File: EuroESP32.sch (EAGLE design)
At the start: 127 parts, among them IC1 TL074D, IC10 MCP6004, IC2 TL072, IC3 TL072, IC4 WM8731, IC5 TL074D, IC7 ADP7118, P4 POWER_SIMPLE10, U1 LM4040SOT23, U2 MCP3204-CI/SL

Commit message: A few corrections
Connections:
- removed net LHPOUT: IC4.LHPOUT
- removed net MICBIAS: IC4.MICBIAS
- removed net MICIN: IC4.MICIN
- removed net RHPOUT: IC4.RHPOUT
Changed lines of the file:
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@@
-</segment>
-</net>
-<net name="LHPOUT" class="0">
-<segment>
-<pinref part="IC4" gate="G$1" pin="LHPOUT"/>
-<wire x1="76.2" y1="-55.88" x2="78.74" y2="-55.88" width="0.1524" layer="91"/>
-<label x="78.74" y="-55.88" size="1.778" layer="95" xref="yes"/>
-</segment>
-</net>
-<net name="RHPOUT" class="0">
-<segment>
-<pinref part="IC4" gate="G$1" pin="RHPOUT"/>
-<wire x1="76.2" y1="-58.42" x2="93.98" y2="-58.42" width="0.1524" layer="91"/>
-<label x="93.98" y="-58.42" size="1.778" layer="95" xref="yes"/>
 </segment>
 </net>
@@
 <wire x1="104.14" y1="-124.46" x2="106.68" y2="-124.46" width="0.1524" layer="91"/>
 <label x="106.68" y="-124.46" size="1.778" layer="95" xref="yes"/>
-</segment>
-</net>
-<net name="MICIN" class="0">
-<segment>
-<pinref part="IC4" gate="G$1" pin="MICIN"/>
-<wire x1="76.2" y1="-71.12" x2="78.74" y2="-71.12" width="0.1524" layer="91"/>
-<label x="78.74" y="-71.12" size="1.778" layer="95" xref="yes"/>
-</segment>
-</net>
-<net name="MICBIAS" class="0">
-<segment>
-<pinref part="IC4" gate="G$1" pin="MICBIAS"/>
-<wire x1="76.2" y1="-73.66" x2="93.98" y2="-73.66" width="0.1524" layer="91"/>
-<label x="93.98" y="-73.66" size="1.778" layer="95" xref="yes"/>
 </segment>
 </net>
@@
 </segment>
 </net>
-<net name="N$7" class="0">
-<segment>
-<pinref part="R21" gate="G$1" pin="1"/>
-<wire x1="421.64" y1="-58.42" x2="416.56" y2="-58.42" width="0.1524" layer="91"/>
-<wire x1="416.56" y1="-58.42" x2="416.56" y2="-68.58" width="0.1524" layer="91"/>
-<pinref part="IC1" gate="B" pin="-IN"/>
-<pinref part="R20" gate="G$1" pin="2"/>
-<wire x1="416.56" y1="-68.58" x2="421.64" y2="-68.58" width="0.1524" layer="91"/>
-<wire x1="411.48" y1="-68.58" x2="416.56" y2="-68.58" width="0.1524" layer="91"/>
-</segment>
-</net>
 <net name="N$8" class="0">
 <segment>
@@
 </segment>
 </net>
-<net name="N$10" class="0">
-<segment>
-<wire x1="421.64" y1="-81.28" x2="416.56" y2="-81.28" width="0.1524" layer="91"/>
-<wire x1="416.56" y1="-81.28" x2="416.56" y2="-91.44" width="0.1524" layer="91"/>
-<wire x1="416.56" y1="-91.44" x2="424.18" y2="-91.44" width="0.1524" layer="91"/>
-<wire x1="411.48" y1="-91.44" x2="416.56" y2="-91.44" width="0.1524" layer="91"/>
-<pinref part="R25" gate="G$1" pin="2"/>
-<pinref part="R26" gate="G$1" pin="1"/>
-<pinref part="IC1" gate="D" pin="-IN"/>
-</segment>
-</net>
 <net name="N$11" class="0">
 <segment>
@@
 </segment>
 </net>
-<net name="N$14" class="0">
-<segment>
-<pinref part="R31" gate="G$1" pin="1"/>
-<wire x1="421.64" y1="-121.92" x2="416.56" y2="-121.92" width="0.1524" layer="91"/>
-<wire x1="416.56" y1="-121.92" x2="416.56" y2="-132.08" width="0.1524" layer="91"/>
-<pinref part="IC5" gate="B" pin="-IN"/>
-<pinref part="R30" gate="G$1" pin="2"/>
-<wire x1="416.56" y1="-132.08" x2="421.64" y2="-132.08" width="0.1524" layer="91"/>
-<wire x1="411.48" y1="-132.08" x2="416.56" y2="-132.08" width="0.1524" layer="91"/>
-</segment>
-</net>
 <net name="N$16" class="0">
 <segment>
@@
 <pinref part="R38" gate="G$1" pin="1"/>
 <pinref part="IC5" gate="D" pin="OUT"/>
-</segment>
-</net>
-<net name="N$22" class="0">
-<segment>
-<wire x1="421.64" y1="-144.78" x2="416.56" y2="-144.78" width="0.1524" layer="91"/>
-<wire x1="416.56" y1="-144.78" x2="416.56" y2="-154.94" width="0.1524" layer="91"/>
-<wire x1="416.56" y1="-154.94" x2="424.18" y2="-154.94" width="0.1524" layer="91"/>
-<wire x1="411.48" y1="-154.94" x2="416.56" y2="-154.94" width="0.1524" layer="91"/>
-<pinref part="R36" gate="G$1" pin="2"/>
-<pinref part="R37" gate="G$1" pin="1"/>
-<pinref part="IC5" gate="D" pin="-IN"/>
 </segment>
 </net>
@@
 </segment>
 </net>
+<net name="N$28" class="0">
+<segment>
+<pinref part="R26" gate="G$1" pin="1"/>
+<wire x1="421.64" y1="-81.28" x2="416.56" y2="-81.28" width="0.1524" layer="91"/>
+<wire x1="411.48" y1="-91.44" x2="416.56" y2="-91.44" width="0.1524" layer="91"/>
+<pinref part="R25" gate="G$1" pin="2"/>
+<pinref part="IC1" gate="D" pin="-IN"/>
+<wire x1="416.56" y1="-91.44" x2="424.18" y2="-91.44" width="0.1524" layer="91"/>
+<wire x1="416.56" y1="-81.28" x2="416.56" y2="-91.44" width="0.1524" layer="91"/>
+<junction x="416.56" y="-91.44"/>
+</segment>
+</net>
+<net name="N$10" class="0">
+<segment>
+<pinref part="R31" gate="G$1" pin="1"/>
+<wire x1="421.64" y1="-121.92" x2="416.56" y2="-121.92" width="0.1524" layer="91"/>
+<pinref part="IC5" gate="B" pin="-IN"/>
+<pinref part="R30" gate="G$1" pin="2"/>
+<wire x1="411.48" y1="-132.08" x2="416.56" y2="-132.08" width="0.1524" layer="91"/>
+<wire x1="416.56" y1="-132.08" x2="421.64" y2="-132.08" width="0.1524" layer="91"/>
+<wire x1="416.56" y1="-121.92" x2="416.56" y2="-132.08" width="0.1524" layer="91"/>
+<junction x="416.56" y="-132.08"/>
+</segment>
+</net>
+<net name="N$14" class="0">
+<segment>
+<pinref part="R37" gate="G$1" pin="1"/>
+<wire x1="421.64" y1="-144.78" x2="416.56" y2="-144.78" width="0.1524" layer="91"/>
+<wire x1="411.48" y1="-154.94" x2="416.56" y2="-154.94" width="0.1524" layer="91"/>
+<pinref part="R36" gate="G$1" pin="2"/>
+<pinref part="IC5" gate="D" pin="-IN"/>
+<wire x1="416.56" y1="-154.94" x2="424.18" y2="-154.94" width="0.1524" layer="91"/>
+<wire x1="416.56" y1="-144.78" x2="416.56" y2="-154.94" width="0.1524" layer="91"/>
+<junction x="416.56" y="-154.94"/>
+</segment>
+</net>
+<net name="N$22" class="0">
+<segment>
+<pinref part="R21" gate="G$1" pin="1"/>
+<wire x1="421.64" y1="-58.42" x2="416.56" y2="-58.42" width="0.1524" layer="91"/>
+<pinref part="IC1" gate="B" pin="-IN"/>
+<pinref part="R20" gate="G$1" pin="2"/>
+<wire x1="411.48" y1="-68.58" x2="416.56" y2="-68.58" width="0.1524" layer="91"/>
+<wire x1="416.56" y1="-68.58" x2="421.64" y2="-68.58" width="0.1524" layer="91"/>
+<wire x1="416.56" y1="-58.42" x2="416.56" y2="-68.58" width="0.1524" layer="91"/>
+<junction x="416.56" y="-68.58"/>
+</segment>
+</net>

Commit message: Added groups in schematic
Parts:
- removed C15, C23, C25: 10uF, parts_aman:CAPACITOR0805
- removed C16, C27, C29, C46: 100nF, parts_aman:CAPACITOR
- removed C43, C45: 1uF, parts_aman:CAPACITOR
- removed REGULATOR: 7805TV, linear:7805TV
- added IC6: 7805T, adafruit:7805T
- C1, C6: device TOF:C2.5/2 -> parts_aman:CAPACITOR1210
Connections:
- net +12V: now also IC6.VI; no longer REGULATOR.VI
- net +3.3VA: no longer C15.1, C16.1, C23.2, C25.2, C27.2, C29.2, C43.2, C45.2, C46.2
- net 5V: now also IC6.VO; no longer REGULATOR.VO
- net GND: now also IC6.GND; no longer C15.2, C16.2, C23.1, C25.1, C27.1, C29.1, C43.1, C45.1, C46.1, REGULATOR.GND
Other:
- moved on the sheet: C1, C10, C11, C12, C13, C14, C17, C18, C19, C20, C24, C30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

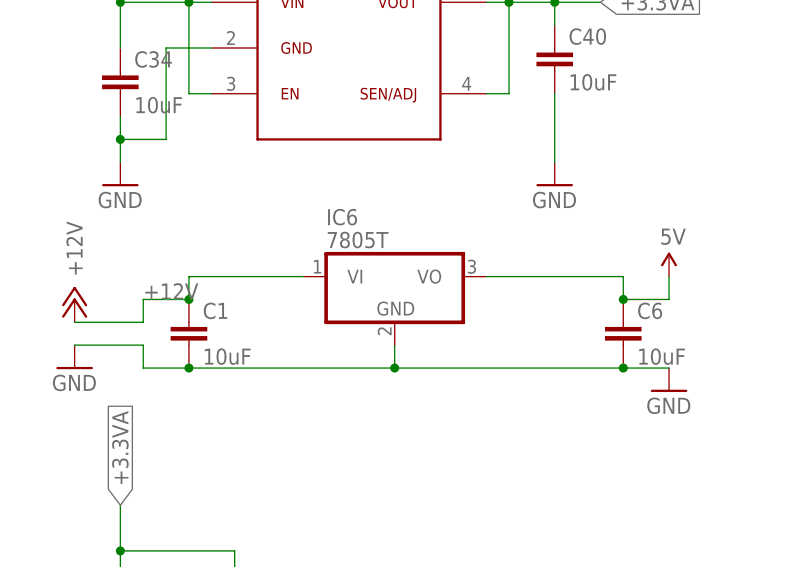
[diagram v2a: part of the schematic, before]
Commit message: Changed voltage regulator
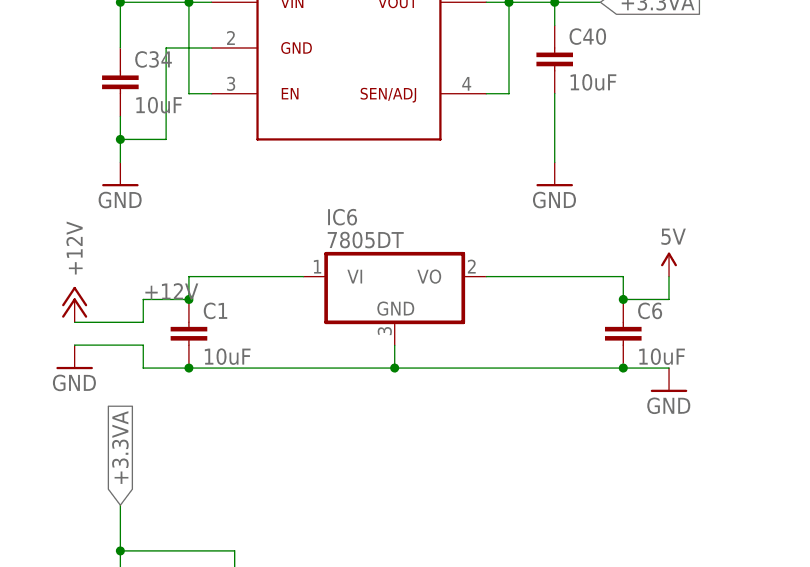
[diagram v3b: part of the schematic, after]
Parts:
- IC6: value 7805T -> 7805DT; device adafruit:7805T -> adafruit:7805DT
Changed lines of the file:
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@@
 <part name="C1" library="parts_aman" deviceset="CAPACITOR" device="1210" value="10uF"/>
 <part name="C6" library="parts_aman" deviceset="CAPACITOR" device="1210" value="10uF"/>
-<part name="IC6" library="adafruit" deviceset="78*" device="T" technology="05"/>
+<part name="IC6" library="adafruit" deviceset="78*" device="DT" technology="05" value="7805DT"/>
 </parts>
 <sheets>

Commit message: Added groups and merged changes from alx-1
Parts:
- removed C30: 100nF, parts_aman:CAPACITOR
- removed C32: 10uF, parts_aman:CAPACITOR0805
- removed H2: PCB_SCREW, parts_aman:PCB_SCREW
- removed IC6: 7805DT, adafruit:7805DT
- added C16: 100nF, parts_aman:CAPACITOR
- added C43: 1uF, parts_aman:CAPACITOR
- added REGULATOR: 7805DT, linear:7805DT
- -10VREF: value -10VREF -> -10V
- CVIN(100K)0: value CVIN(100k)0 -> CVI0
- CVIN(100K)1: value CVIN(100K)1 -> CVI1
- CVIN(100K)2: value CVIN(100K)2 -> CVI2
- CVIN(100K)3: value CVIN(100K)3 -> CVI3
- CVOUT1: value CVOUT1 -> CVO1
- CVOUT2: value CVOUT2 -> CVO2
- CVOUT3: value CVOUT3 -> CVO3
- CVOUT4: value CVOUT4 -> CVO4
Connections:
- net +12V: now also REGULATOR.VI; no longer IC6.VI
- net +3.3VA: now also C16.1, C43.2; no longer C30.2, C32.1
- net 5V: now also REGULATOR.VO; no longer IC6.VO
- net GND: now also C16.2, C43.1, REGULATOR.GND; no longer C30.1, C32.2, IC6.GND
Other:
- moved on the sheet: +12V, +3.3VA, -12V, C1, C10, C11, C12, C13, C14, C17, C18, C19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

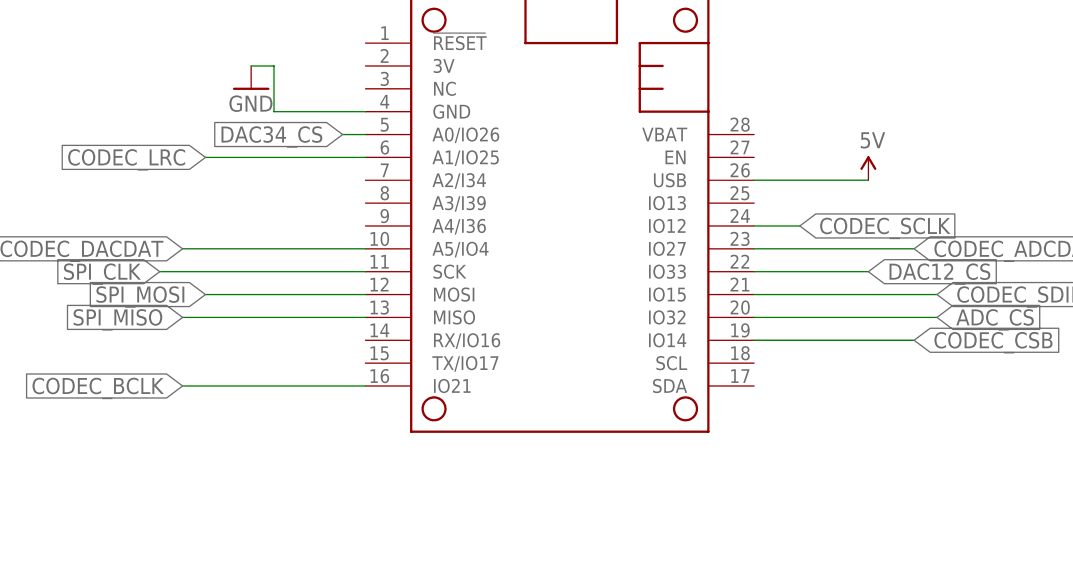
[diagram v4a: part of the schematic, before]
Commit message: Added extra connectors
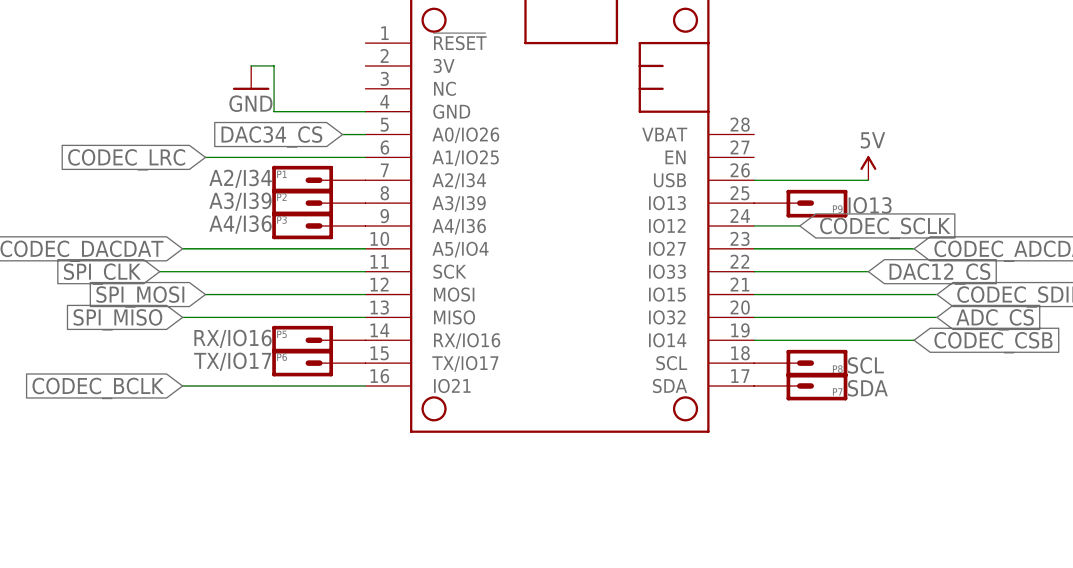
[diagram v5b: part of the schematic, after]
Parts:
- added P1: A2/I34, TOF:HEADER-1X1
- added P2: A3/I39, TOF:HEADER-1X1
- added P3: A4/I36, TOF:HEADER-1X1
- added P5: RX/IO16, TOF:HEADER-1X1
- added P6: TX/IO17, TOF:HEADER-1X1
- added P7: SDA, TOF:HEADER-1X1
- added P8: SCL, TOF:HEADER-1X1
- added P9: IO13, TOF:HEADER-1X1
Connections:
- new net N$30: MS2.A3/I39, P2.1
- new net N$35: MS2.A4/I36, P3.1
- new net N$38: MS2.RX/IO16, P5.1
- new net N$39: MS2.TX/IO17, P6.1
- new net N$41: MS2.SDA, P7.1
- new net N$50: MS2.SCL, P8.1
- new net N$51: MS2.IO13, P9.1
- new net N$7: MS2.A2/I34, P1.1

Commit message: Added a little information
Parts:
- D1, D2: value (none) -> 1N5819HW
- F1, F2: value FERRITE-BEAD0805 -> Würth Electronics 742792664
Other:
- note added: "ADC IN -5V to +5V TO MCU +3V3 to 0V (INVERTED)"
- note removed: "ADC IN -5V to +5V TO MCU 0V to +3V3"
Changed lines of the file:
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@@
 <part name="GND26" library="parts_aman" deviceset="GND" device=""/>
 <part name="P4" library="parts_aman" deviceset="POWER_SIMPLE" device="10"/>
-<part name="D1" library="parts_aman" deviceset="DIODE" device=""/>
-<part name="D2" library="parts_aman" deviceset="DIODE" device=""/>
-<part name="F1" library="parts_aman" deviceset="FERRITE-BEAD" device="0805" value="FERRITE-BEAD0805"/>
-<part name="F2" library="parts_aman" deviceset="FERRITE-BEAD" device="0805" value="FERRITE-BEAD0805"/>
+<part name="D1" library="parts_aman" deviceset="DIODE" device="" value="1N5819HW"/>
+<part name="D2" library="parts_aman" deviceset="DIODE" device="" value="1N5819HW"/>
+<part name="F1" library="parts_aman" deviceset="FERRITE-BEAD" device="0805" value="Würth Electronics 742792664"/>
+<part name="F2" library="parts_aman" deviceset="FERRITE-BEAD" device="0805" value="Würth Electronics 742792664"/>
 <part name="P+4" library="parts_aman" deviceset="+12V" device=""/>
 <part name="P-2" library="parts_aman" deviceset="-12V" device=""/>
@@
 <sheet>
 <plain>
-<text x="241.3" y="86.36" size="1.778" layer="97" grouprefs="CV_IN">ADC IN -5V to +5V TO MCU 0V to +3V3</text>
+<text x="241.3" y="86.36" size="1.778" layer="97" grouprefs="CV_IN">ADC IN -5V to +5V TO MCU +3V3 to 0V (INVERTED)</text>
 </plain>
 <instances>
